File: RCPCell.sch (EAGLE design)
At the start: 18 parts, among them IC1 SIM900, U1 PESDXS4UD

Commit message: laid out power supply section, fixed DRC errors
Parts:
- removed C11: 47uF, rcl:CPOL-USSMCD
- added C2: 47uF, rcl:CPOL-USSMCD
- added C39, C42: 0.01uF, rcl:C-USC0603
- added C40: 560pF, rcl:C-USC0603
- added D25: SCHOTTKY, smt_diodes:SCHOTTKY
- added L3: CD54, sumida_inductors:CD54
- added R49: 43K, rcl:R-US_R0603
- added R50: 24K 1%, rcl:R-US_R0603
- added R51: 2.43K 1%, rcl:R-US_R0603
- added U7: FAN8303, voltage_regulators:FAN8303
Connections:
- new net +6V: R50.1
- new net N$1000: C39.1, D25.C, L3.2, U7.SW
- new net N$1100: C40.2, R49.2
- new net N$1200: R49.1, U7.COMP
- new net N$1300: C42.2, U7.SS
- new net N$800: R50.2, R51.1, U7.FB
- new net N$900: C39.2, U7.BS
- net GND: now also C2.-, C40.1, C42.1, D25.A, R51.2, U7.GND; no longer C11.-
- net SAFE12V: now also C2.+, U7.VIN; no longer C11.+
- net V+: now also L3.1
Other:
- moved on the sheet: C10, C12, C7, C8, C9, EX1, EX2, IC1

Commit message: tentative final version of RevC module
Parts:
- added R4: 1k, SparkFun:RESISTOR0603
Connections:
- removed net +5V: EX2.3, EX2.4
- removed net PWRKEY_OUT: IC1G$1.PWRKEY_OUT
- removed net RXD3: EX1.6
- removed net TXD3: EX1.5
- new net EXT_CTRL: EX1.2, R4.2
- net DIN: now also EX1.5
- net DOUT: now also EX1.6
- net PWRKEY: now also R4.1
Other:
- note added: "C"
- note removed: "B"
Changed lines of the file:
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@@
 <setting verticaltext="up"/>
 </settings>
-<grid distance="0.1" unitdist="inch" unit="inch" style="lines" multiple="1" display="no" altdistance="0.01" altunitdist="inch" altunit="inch"/>
+<grid distance="0.01" unitdist="inch" unit="inch" style="lines" multiple="1" display="no" altdistance="0.01" altunitdist="inch" altunit="inch"/>
 <layers>
 <layer number="1" name="Top" color="4" fill="1" visible="no" active="no"/>
@@
 <part name="NETLIGHT" library="LEDs" deviceset="PANEL_LED" device=""/>
 <part name="C10" library="rcl" deviceset="CPOL-US" device="SMCD" value="47uF"/>
-<part name="AD74" library="supply2" deviceset="V--&gt;" device="" value=""/>
-<part name="AD76" library="supply2" deviceset="V--&gt;" device="" value=""/>
 <part name="C12" library="rcl" deviceset="C-US" device="C0603" value="0.1uf"/>
 <part name="IC1" library="sim900" deviceset="SIM900" device=""/>
@@
 <part name="GND2" library="supply1" deviceset="GND" device=""/>
 <part name="AD5" library="supply2" deviceset="V--&gt;" device="" value=""/>
-<part name="AD6" library="supply2" deviceset="V--&gt;" device="" value=""/>
 <part name="AD7" library="supply2" deviceset="V--&gt;" device="" value=""/>
 <part name="C9" library="rcl" deviceset="CPOL-US" device="SMCD" value="47uF"/>
@@
 <part name="AD137" library="supply2" deviceset="V--&gt;" device="" value=""/>
 <part name="AD151" library="supply2" deviceset="V--&gt;" device="" value=""/>
-<part name="P+37" library="supply1" deviceset="+5V" device=""/>
 <part name="GND82" library="supply1" deviceset="GND" device=""/>
 <part name="GND83" library="supply1" deviceset="GND" device=""/>
@@
 <part name="P+2" library="supply1" deviceset="+5V" device="" value="+6V"/>
 <part name="C2" library="rcl" deviceset="CPOL-US" device="SMCD" value="47uF"/>
+<part name="AD1" library="supply2" deviceset="V--&gt;" device="" value=""/>
+<part name="R4" library="SparkFun" deviceset="RESISTOR" device="0603" value="1k"/>
+<part name="AD2" library="supply2" deviceset="V--&gt;" device="" value=""/>
 </parts>
 <sheets>
@@
 <text x="200.66" y="190.5" size="6.4516" layer="97" rot="R180">RaceCapture Cell Telemetry</text>
 <text x="113.03" y="201.803" size="6.4516" layer="97" font="vector">autosportlabs.com</text>
-<text x="195.326" y="-34.544" size="3.81" layer="97" ratio="5">B</text>
+<text x="195.326" y="-34.544" size="3.81" layer="97" ratio="5">C</text>
 <rectangle x1="132.2705" y1="210.8835" x2="203.1365" y2="211.0105" layer="97"/>
 <rectangle x1="132.2705" y1="211.0105" x2="203.1365" y2="211.1375" layer="97"/>
@@
 <instance part="NETLIGHT" gate="G$1" x="-187.96" y="9.144"/>
 <instance part="C10" gate="G$1" x="13.462" y="35.56"/>
-<instance part="AD74" gate="G$1" x="27.686" y="-12.7" smashed="yes" rot="R180">
-<attribute name="VALUE" x="26.416" y="-11.938" size="1.778" layer="96" rot="R180"/>
-</instance>
-<instance part="AD76" gate="G$1" x="27.686" y="-17.78" smashed="yes" rot="R180">
-<attribute name="VALUE" x="26.416" y="-17.018" size="1.778" layer="96" rot="R180"/>
-</instance>
 <instance part="C12" gate="G$1" x="-41.91" y="60.96" smashed="yes">
 <attribute name="NAME" x="-35.306" y="62.865" size="1.778" layer="95" rot="R180"/>
@@
 </instance>
 <instance part="GND2" gate="1" x="-127" y="170.18"/>
-<instance part="AD5" gate="G$1" x="-45.974" y="-17.78" smashed="yes" rot="R180">
-<attribute name="VALUE" x="-47.244" y="-17.018" size="1.778" layer="96" rot="R180"/>
-</instance>
-<instance part="AD6" gate="G$1" x="-150.114" y="147.32" smashed="yes" rot="R180">
-<attribute name="VALUE" x="-151.384" y="148.082" size="1.778" layer="96" rot="R180"/>
+<instance part="AD5" gate="G$1" x="-17.272" y="-18.542" smashed="yes">
+<attribute name="VALUE" x="-16.002" y="-19.304" size="1.778" layer="96"/>
 </instance>
 <instance part="AD7" gate="G$1" x="-150.114" y="149.86" smashed="yes" rot="R180">
@@
 <attribute name="VALUE" x="-97.536" y="-3.302" size="1.778" layer="96"/>
 </instance>
-<instance part="P+37" gate="1" x="-134.62" y="12.7" smashed="yes">
-<attribute name="VALUE" x="-129.032" y="13.716" size="1.778" layer="96" rot="R180"/>
-</instance>
 <instance part="GND82" gate="1" x="-99.06" y="-17.78"/>
 <instance part="GND83" gate="1" x="-149.86" y="-17.78"/>
@@
 </instance>
 <instance part="C2" gate="G$1" x="-27.94" y="60.96"/>
+<instance part="AD1" gate="G$1" x="-98.806" y="-5.08" smashed="yes">
+<attribute name="VALUE" x="-97.536" y="-5.842" size="1.778" layer="96"/>
+</instance>
+<instance part="R4" gate="G$1" x="-33.782" y="-18.542" rot="R180"/>
+<instance part="AD2" gate="G$1" x="-48.006" y="-18.542" smashed="yes" rot="R180">
+<attribute name="VALUE" x="-49.276" y="-17.78" size="1.778" layer="96" rot="R180"/>
+</instance>
 </instances>
 <busses>
@@
 <net name="DIN" class="0">
 <segment>
-<wire x1="33.02" y1="-17.78" x2="27.94" y2="-17.78" width="0.1524" layer="91"/>
-<label x="20.828" y="-18.542" size="1.778" layer="95"/>
-</segment>
-<segment>
 <wire x1="-137.16" y1="127" x2="-149.86" y2="127" width="0.1524" layer="91"/>
 <label x="-150.622" y="127.762" size="1.778" layer="95" rot="R180"/>
 <pinref part="IC1" gate="G$1" pin="RXD"/>
 </segment>
+<segment>
+<pinref part="EX1" gate="1" pin="5"/>
+<wire x1="-106.68" y1="2.54" x2="-99.06" y2="2.54" width="0.1524" layer="91"/>
+<label x="-98.298" y="1.778" size="1.778" layer="95"/>
+</segment>
 </net>
 <net name="DOUT" class="0">
-<segment>
-<wire x1="33.02" y1="-12.7" x2="27.94" y2="-12.7" width="0.1524" layer="91"/>
-<label x="20.828" y="-13.462" size="1.778" layer="95"/>
-</segment>
 <segment>
 <wire x1="-137.16" y1="129.54" x2="-149.86" y2="129.54" width="0.1524" layer="91"/>
 <label x="-150.622" y="130.302" size="1.778" layer="95" rot="R180"/>
 <pinref part="IC1" gate="G$1" pin="TXD"/>
+</segment>
+<segment>
+<pinref part="EX1" gate="1" pin="6"/>
+<wire x1="-106.68" y1="5.08" x2="-99.06" y2="5.08" width="0.1524" layer="91"/>
+<label x="-98.298" y="4.318" size="1.778" layer="95"/>
 </segment>
 </net>
@@
 </segment>
 </net>
-<net name="+5V" class="0">
-<segment>
-<pinref part="EX2" gate="1" pin="3"/>
-<wire x1="-157.48" y1="-2.54" x2="-134.62" y2="-2.54" width="0.1524" layer="91"/>
-<wire x1="-134.62" y1="-2.54" x2="-134.62" y2="0" width="0.1524" layer="91"/>
-<pinref part="P+37" gate="1" pin="+5V"/>
-<pinref part="EX2" gate="1" pin="4"/>
-<wire x1="-134.62" y1="0" x2="-134.62" y2="10.16" width="0.1524" layer="91"/>
-<wire x1="-157.48" y1="0" x2="-134.62" y2="0" width="0.1524" layer="91"/>
-<junction x="-134.62" y="0"/>
-</segment>
-</net>
 <net name="RF_ANT" class="0">
 <segment>
@@
 </segment>
 <segment>
-<wire x1="-15.24" y1="-17.78" x2="-45.72" y2="-17.78" width="0.1524" layer="91"/>
-<label x="-45.974" y="-16.764" size="1.778" layer="95" rot="R180"/>
-</segment>
-</net>
-<net name="PWRKEY_OUT" class="0">
-<segment>
-<wire x1="-137.16" y1="147.32" x2="-149.86" y2="147.32" width="0.1524" layer="91"/>
-<label x="-150.876" y="148.336" size="1.778" layer="95" rot="R180"/>
-<pinref part="IC1" gate="G$1" pin="PWRKEY_OUT"/>
+<wire x1="-28.702" y1="-18.542" x2="-17.526" y2="-18.542" width="0.1524" layer="91"/>
+<label x="-17.272" y="-19.558" size="1.778" layer="95"/>
+<pinref part="R4" gate="G$1" pin="1"/>
 </segment>
 </net>
@@
 </segment>
 </net>
-<net name="TXD3" class="0">
-<segment>
-<pinref part="EX1" gate="1" pin="5"/>
-<wire x1="-106.68" y1="2.54" x2="-99.06" y2="2.54" width="0.1524" layer="91"/>
-<label x="-98.298" y="1.778" size="1.778" layer="95"/>
-</segment>
-</net>
-<net name="RXD3" class="0">
-<segment>
-<pinref part="EX1" gate="1" pin="6"/>
-<wire x1="-106.68" y1="5.08" x2="-99.06" y2="5.08" width="0.1524" layer="91"/>
-<label x="-98.298" y="4.318" size="1.778" layer="95"/>
-</segment>
-</net>
 <net name="USB_DM_HS_OUT" class="0">
 <segment>
@@
 </segment>
 </net>
+<net name="EXT_CTRL" class="0">
+<segment>
+<pinref part="EX1" gate="1" pin="2"/>
+<wire x1="-106.68" y1="-5.08" x2="-99.06" y2="-5.08" width="0.1524" layer="91"/>
+<label x="-98.298" y="-5.842" size="1.778" layer="95"/>
+</segment>
+<segment>
+<pinref part="R4" gate="G$1" pin="2"/>
+<wire x1="-38.862" y1="-18.542" x2="-48.006" y2="-18.542" width="0.1524" layer="91"/>
+<label x="-48.514" y="-17.526" size="1.778" layer="95" rot="R180"/>
+</segment>
+</net>

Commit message: yak shaving design a bit
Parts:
- R51: value 2.43K 1% -> 3.9K 1%
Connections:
- net GND renamed N$2
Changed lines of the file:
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@@
 <setting verticaltext="up"/>
 </settings>
-<grid distance="0.01" unitdist="inch" unit="inch" style="lines" multiple="1" display="no" altdistance="0.01" altunitdist="inch" altunit="inch"/>
+<grid distance="0.1" unitdist="inch" unit="inch" style="lines" multiple="1" display="no" altdistance="0.01" altunitdist="inch" altunit="inch"/>
 <layers>
 <layer number="1" name="Top" color="4" fill="1" visible="no" active="no"/>
@@
 <part name="D25" library="smt_diodes" deviceset="SCHOTTKY" device=""/>
 <part name="R50" library="rcl" deviceset="R-US_" device="R0603" value="24K 1%"/>
-<part name="R51" library="rcl" deviceset="R-US_" device="R0603" value="2.43K 1%"/>
+<part name="R51" library="rcl" deviceset="R-US_" device="R0603" value="3.9K 1%"/>
 <part name="U7" library="voltage_regulators" deviceset="FAN8303" device=""/>
 <part name="C39" library="rcl" deviceset="C-US" device="C0603" value="0.01uF"/>
@@
 </busses>
 <nets>
-<net name="GND" class="0">
+<net name="N$2" class="0">
 <segment>
 <wire x1="-208.28" y1="213.36" x2="-200.66" y2="213.36" width="0.1524" layer="91"/>

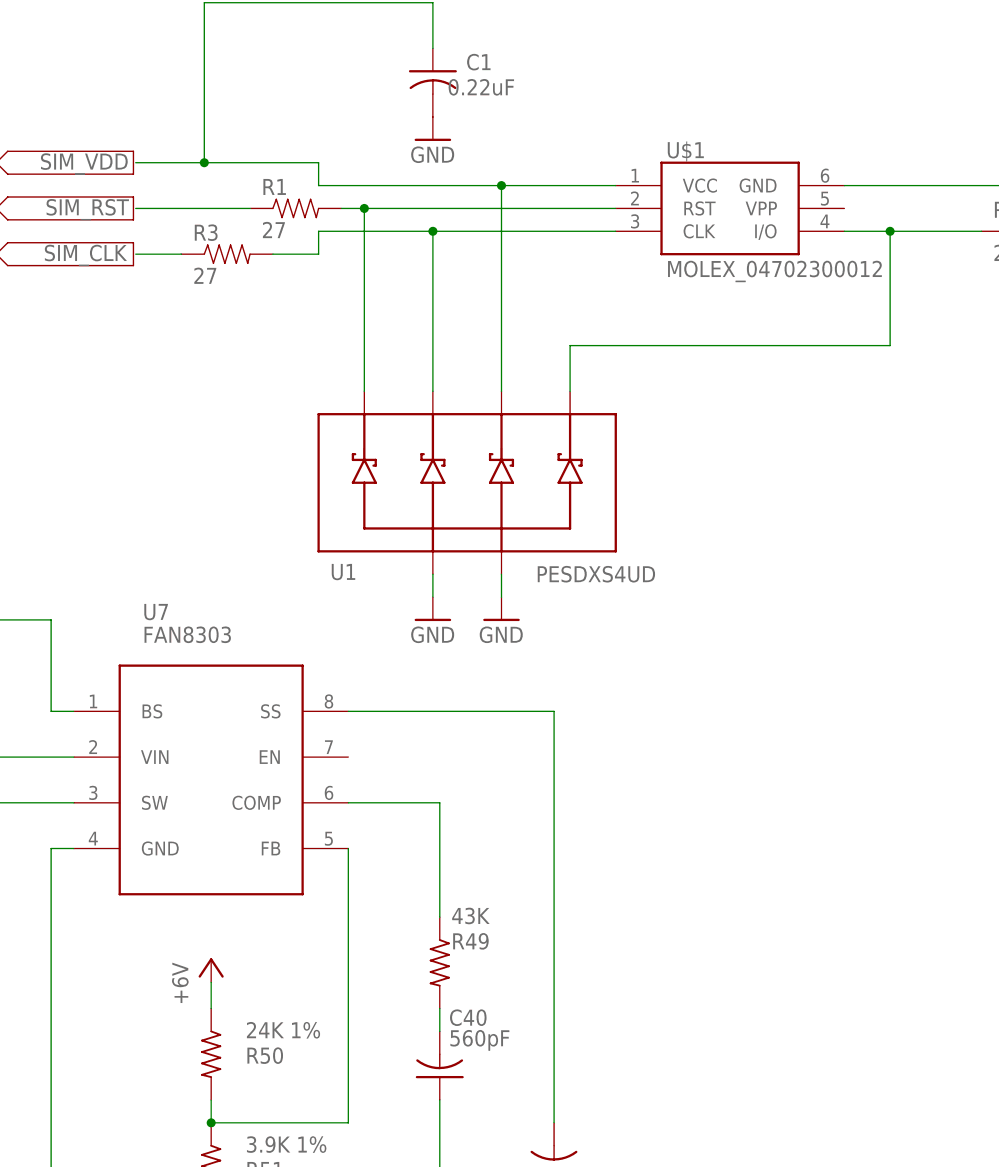
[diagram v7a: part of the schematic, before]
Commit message: WIP for flipping cell module components over
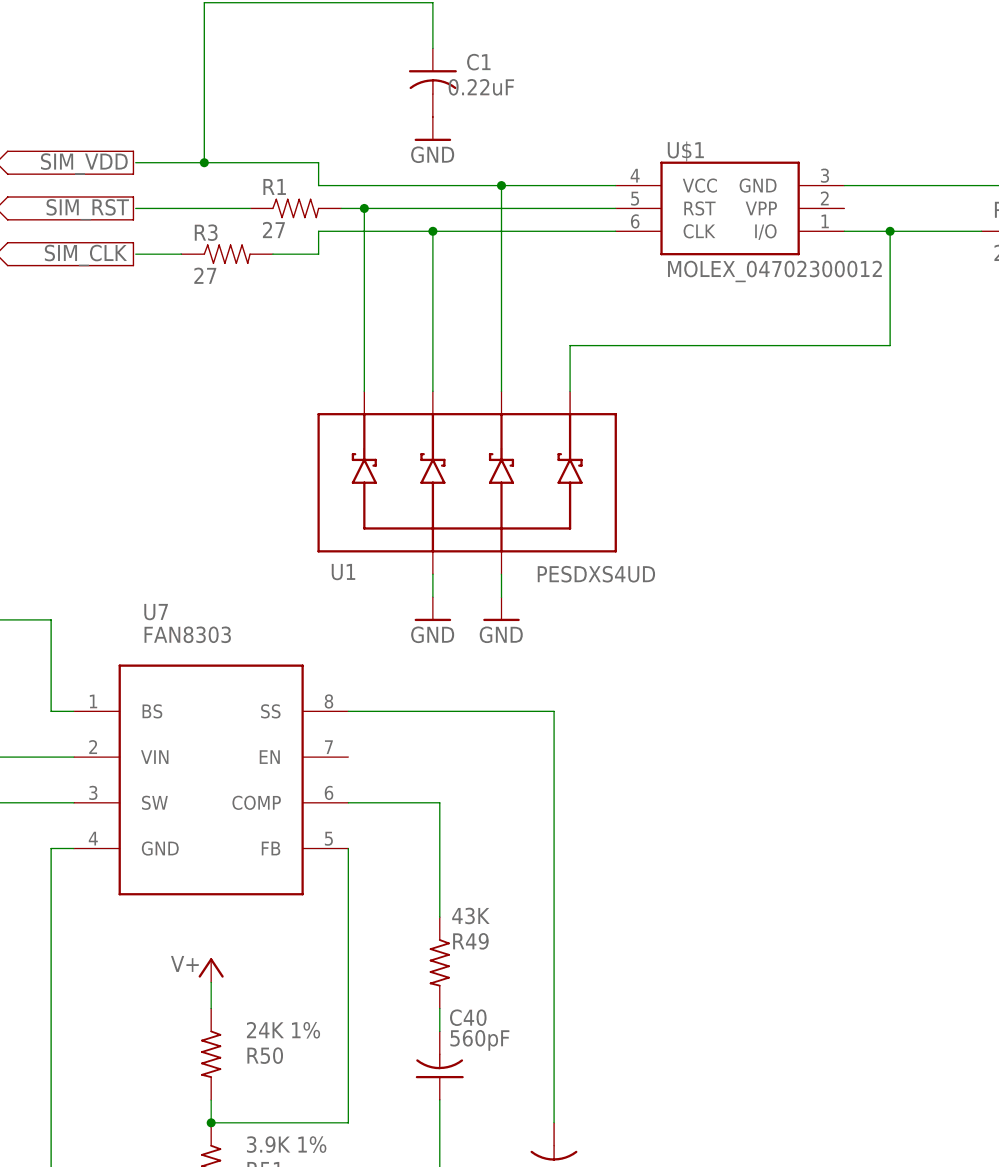
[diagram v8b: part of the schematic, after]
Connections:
- removed net +6V: R50.1
- new net GND: C10.-, C12.2, C2.-, C40.1, C42.1, C7.2, C8.-, C9.-, D25.A, R51.2, U7.GND
- net N$2: no longer C10.-, C12.2, C2.-, C40.1, C42.1, C7.2, C8.-, C9.-, D25.A, R51.2, U7.GND
- net V+: now also R50.1
